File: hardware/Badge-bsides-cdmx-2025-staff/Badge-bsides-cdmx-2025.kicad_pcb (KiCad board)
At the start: 2 copper layers, 50 x 110 mm, 30 parts, among them J1 SWDIO, J3 ADDON, J4 Conn_01x04_Pin, J5 I2C, J6 Conn_01x04_Pin, P6 USB_C_Plug_USB2.0, Q3 DMG3415U-7, SW11 ON, SW2 RESET, U1 PY32F030F28U6TR, U6 AP2112K-3.3

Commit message: feat(Hw):started_routing
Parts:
- added C67: 10uF, Capacitor_SMD:C_0603_1608Metric, B.Cu at (138.6, 53.6)
- added C68: 10uF, Capacitor_SMD:C_0603_1608Metric, B.Cu at (130.4, 73.0)
- added C69: 10uF, Capacitor_SMD:C_0603_1608Metric, B.Cu at (122.8, 54.7)
- added C70: 10uF, Capacitor_SMD:C_0603_1608Metric, B.Cu at (115.0, 74.5)
- added R5: 10k, Resistor_SMD:R_0603_1608Metric, B.Cu at (138.6, 55.1)
- added R6: 10k, Resistor_SMD:R_0603_1608Metric, B.Cu at (130.4, 74.5)
- added R7: 10k, Resistor_SMD:R_0603_1608Metric, B.Cu at (122.8, 53.2)
- added R8: 10k, Resistor_SMD:R_0603_1608Metric, B.Cu at (115.0, 73.0)
- added SW10: SW_Push, Footprints:TS1088R02026, F.Cu at (115.1, 73.7)
- added SW7: SW_Push, Footprints:TS1088R02026, F.Cu at (122.8, 54.1)
- added SW8: SW_Push, Footprints:TS1088R02026, F.Cu at (138.6, 54.2)
- added SW9: SW_Push, Footprints:TS1088R02026, F.Cu at (130.5, 73.7)
- added kibuzzard-6841BD6C: G***, kibuzzard-6841BD6C, B.Cu at (129.0, 141.0)
- BT3, BT4: moved to B.Cu
- J3: moved to F.Cu
- J4: footprint Connector_PinHeader_2.54mm:PinHeader_1x04_P2.54mm_Vertical -> Connector_PinHeader_2.54mm:PinHeader_1x04_P2.54mm_Horizontal; moved to B.Cu
- J6: footprint Connector_PinHeader_2.54mm:PinHeader_1x04_P2.54mm_Vertical -> Connector_PinSocket_2.54mm:PinSocket_1x04_P2.54mm_Horizontal; moved to B.Cu
- moved J1 64.0 mm to (107.9, 84.3)
- moved J3 39.5 mm to (110.9, 46.0), turned to 90 degrees
- moved R4 23.4 mm to (135.2, 81.9)
- moved SW2 23.4 mm to (130.1, 83.4)
- moved C6 23.4 mm to (127.3, 79.6)
- moved J4 23.1 mm to (150.3, 97.5)
- moved J5 21.6 mm to (107.9, 60.7)
- moved R9 20.5 mm to (122.3, 118.5), turned to 0 degrees
- moved R10 20.1 mm to (110.7, 115.8)
- moved R41 20.1 mm to (149.2, 103.9)
- moved U1 20.1 mm to (129.6, 92.4)
- moved C10 20.1 mm to (117.7, 109.2)
- moved C26 20.1 mm to (122.0, 107.7)
- moved Q3 20.1 mm to (113.6, 115.9)
- moved SW11 20.1 mm to (108.4, 110.2)
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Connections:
- J3 pad 5: /GPIO1 -> /GPIO2
- J3 pad 6: /GPIO2 -> /GPIO1
- J4 pad 1: /RX -> GND
- J4 pad 2: /RX -> GND
- J4 pad 3: GND -> /RX
- J4 pad 4: GND -> /RX
- J6 pad 1: /TX -> GND
- J6 pad 2: /TX -> GND
- J6 pad 3: GND -> /TX
- J6 pad 4: GND -> /TX
- U1 pad 1: unconnected-(U1-PA5-Pad1) -> /BTTN2
- U1 pad 10: unconnected-(U1-PB6-Pad10) -> /LED1
- U1 pad 16: /GPIO2 -> /BTTN4
- U1 pad 17: /GPIO1 -> /BTTN3
- U1 pad 2: /LED1 -> /BTTN1
- U1 pad 20: unconnected-(U1-PA4-Pad20) -> /LED2
- U1 pad 3: /LED2 -> /GPIO1
- U1 pad 5: unconnected-(U1-PA12-Pad5) -> /GPIO2
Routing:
- net /BTTN3: track 0.00 -> 43.4 mm, vias 0 -> 1
- net VBUS: track 7.00 -> 40.2 mm, vias 0 -> 2
- net /BTTN2: track 0.00 -> 32.3 mm, vias 0 -> 2
- net /BTTN4: track 0.00 -> 31.3 mm, vias 0 -> 1
- net /LED2: track 0.00 -> 26.1 mm
- net /NTST: track 0.00 -> 25.0 mm, vias 0 -> 2
- net /BTTN1: track 0.00 -> 23.1 mm, vias 0 -> 1
- net /TX: track 0.00 -> 8.26 mm, vias 0 -> 1
- net /SDA: track 0.00 -> 6.40 mm, vias 0 -> 1
- net Net-(D4-K): track 3.60 -> 9.51 mm
- net Net-(D10-K): track 0.00 -> 3.98 mm
- net GND: track 0.00 -> 1.70 mm
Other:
- board size 50 x 110 mm -> 50.1 x 110 mm

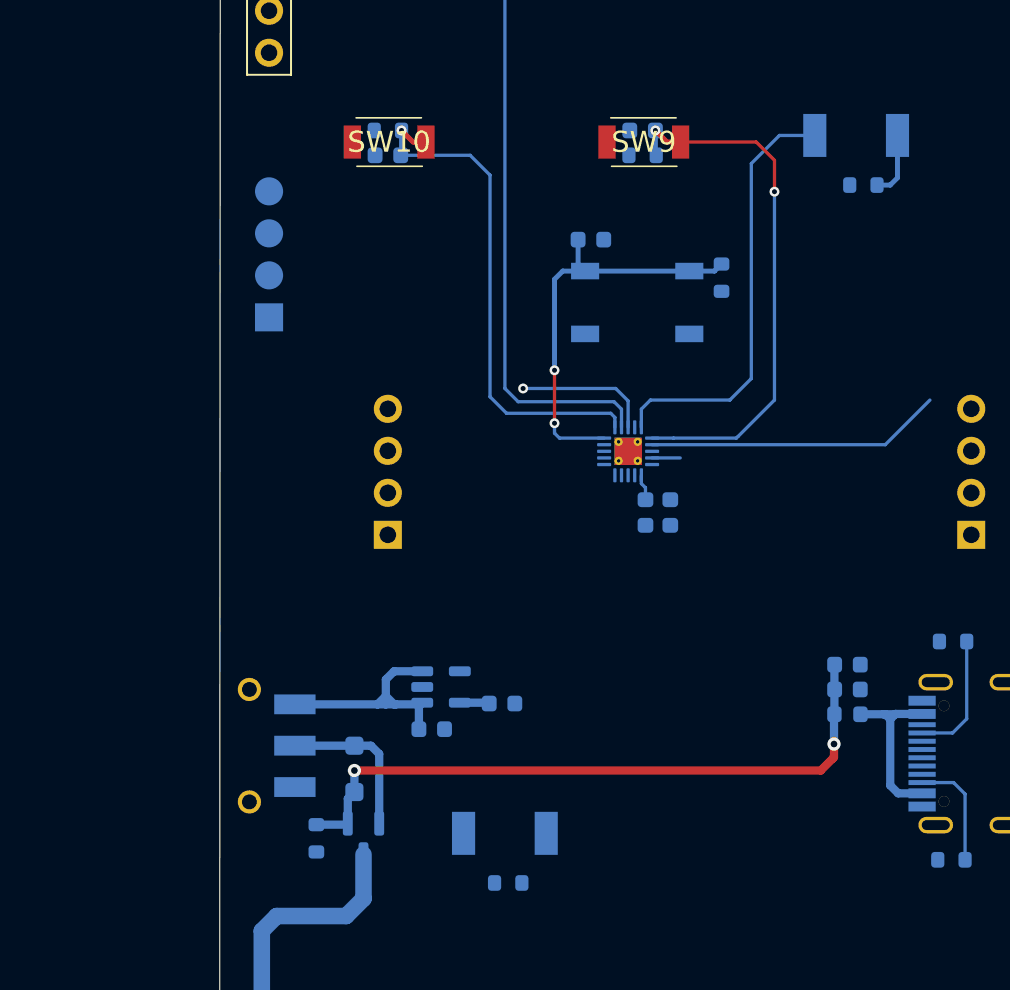
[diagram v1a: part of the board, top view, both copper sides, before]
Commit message: feat(Hw):Neopixels_Added_Staff
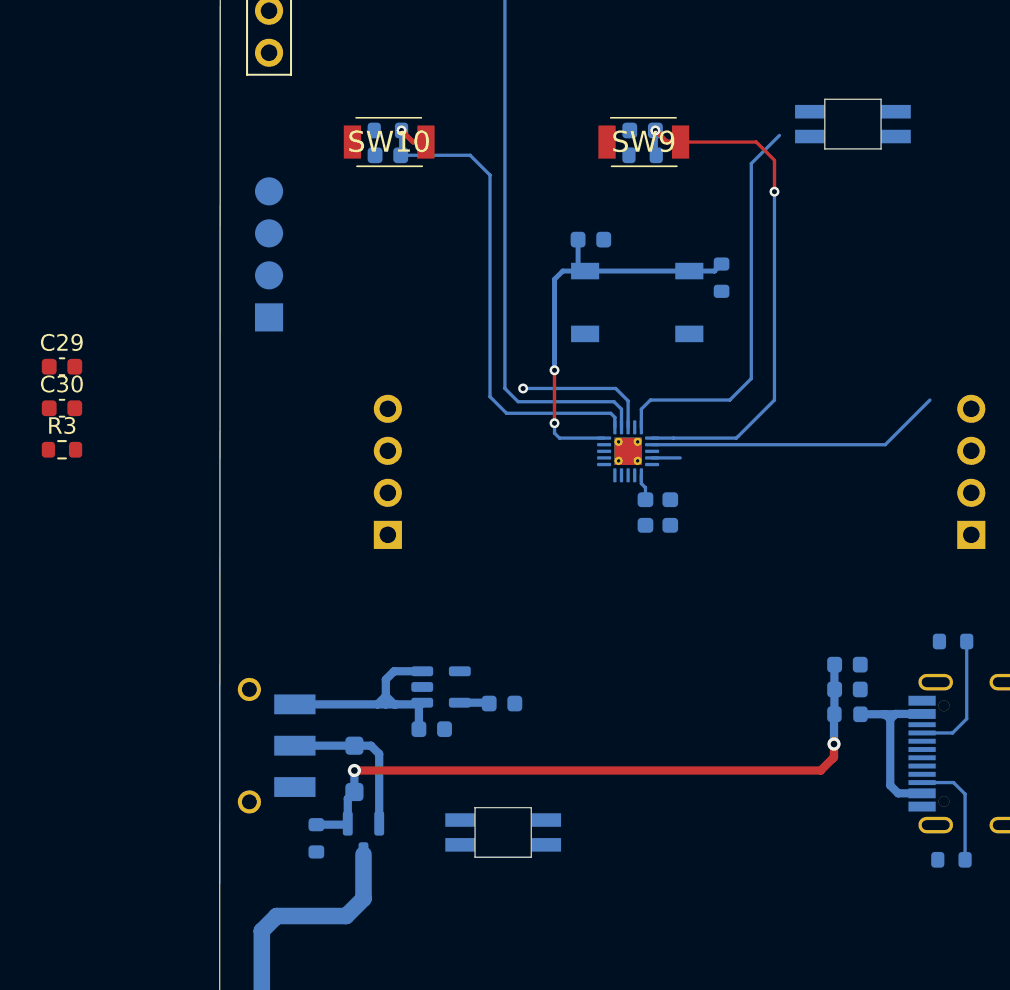
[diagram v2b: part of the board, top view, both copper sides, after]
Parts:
- removed D10, D9: R_LED, Footprints:LYT77K-K2M1
- removed R11, R9: 220, Resistor_SMD:R_0603_1608Metric
- added C29: 100nF, Capacitor_SMD:C_0603_1608Metric, F.Cu at (95.3, 87.3)
- added C30: 100nF, Capacitor_SMD:C_0603_1608Metric, F.Cu at (95.3, 89.8)
- added D19: WS2812B, Footprints:LED_SK6812-E, B.Cu at (143.2, 72.6)
- added D20: WS2812B, Footprints:LED_SK6812-E, B.Cu at (122.0, 115.5)
- added R3: 1K, Resistor_SMD:R_0603_1608Metric, F.Cu at (95.3, 92.3)
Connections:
- BT3 pad 1: Net-(BT3--) -> +BATT
- BT3 pad 2: +BATT -> Net-(BT3--)
- C26 pad 1: +3V3 -> +3.3V
- J3 pad 1: +3V3 -> +3.3V
- R4 pad 2: +3V3 -> +3.3V
- R5 pad 2: +3V3 -> +3.3V
- R6 pad 2: +3V3 -> +3.3V
- R7 pad 2: +3V3 -> +3.3V
- R8 pad 2: +3V3 -> +3.3V
- U1 pad 11: unconnected-(U1-PB7-Pad11) -> /GPIO1
- U1 pad 3: /GPIO1 -> /NEO
- U6 pad 5: +3V3 -> +3.3V
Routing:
- net Net-(D10-K): track 3.98 -> 0.00 mm
- net /LED2: track 26.1 -> 23.9 mm
- net +3V3: track 1.80 -> 0.00 mm
- net +3.3V: track 1.65 -> 3.44 mm

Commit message: feat(HW):Staff_Updated
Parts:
- added kibuzzard-684362A9: G***, kibuzzard-684362A9, B.Cu at (110.5, 105.1)
- added kibuzzard-684362BF: G***, kibuzzard-684362BF, B.Cu at (108.6, 116.2)
- added kibuzzard-684362CB: G***, kibuzzard-684362CB, B.Cu at (114.7, 100.8)
- added kibuzzard-684362D8: G***, kibuzzard-684362D8, B.Cu at (151.2, 100.8)
- added kibuzzard-684362E4: G***, kibuzzard-684362E4, B.Cu at (148.1, 61.6)
- C29, C30, R3: moved to B.Cu
- moved R3 57.0 mm to (148.5, 71.6), turned to 180 degrees
- moved C29 48.7 mm to (140.9, 70.1)
- moved BT4 44.7 mm to (107.4, 142.9), turned to 0 degrees
- moved C30 32.9 mm to (118.8, 113.0), turned to 180 degrees
- moved SW2 31.1 mm to (147.7, 57.8)
- moved SW8 26.9 mm to (145.4, 80.2)
- moved SW7 26.2 mm to (124.6, 80.2), turned to 0 degrees
- moved C6 25.2 mm to (144.9, 61.5)
- moved C67 23.8 mm to (148.2, 75.4)
- moved R5 23.8 mm to (148.2, 76.9)
- moved R7 21.9 mm to (122.4, 75.1), turned to 180 degrees
- moved C69 21.9 mm to (122.5, 76.6), turned to 180 degrees
- moved R4 21.2 mm to (144.9, 63.1), turned to 0 degrees
- moved SW9 7.91 mm to (135.0, 80.2)
- moved C68 6.70 mm to (136.7, 75.4)
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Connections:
- BT4 pad 1: GND -> Net-(BT3--)
- BT4 pad 2: Net-(BT3--) -> GND
- J4 pad 3: /RX -> /TX
- J4 pad 4: /RX -> /TX
- J6 pad 3: /TX -> /RX
- J6 pad 4: /TX -> /RX
- U1 pad 10: /LED1 -> unconnected-(U1-PB6-Pad10)
- U1 pad 12: unconnected-(U1-PF4/BOOT0-Pad12) -> /GPIO2
- U1 pad 20: /LED2 -> unconnected-(U1-PA4-Pad20)
- U1 pad 5: /GPIO2 -> unconnected-(U1-PA12-Pad5)
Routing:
- net +3.3V: track 3.44 -> 171.4 mm, vias 0 -> 6
- net /GPIO2: track 0.00 -> 77.8 mm, vias 0 -> 1
- net /GPIO1: track 0.00 -> 69.9 mm, vias 0 -> 1
- net /SCL: track 0.03 -> 64.2 mm
- net /SDA: track 6.40 -> 69.2 mm, vias 1 -> 0
- net Net-(D19-DOUT): track 0.00 -> 55.8 mm, vias 0 -> 2
- net Net-(BT3--): track 55.1 -> 14.1 mm
- net VBUS: track 40.2 -> 80.8 mm
- net /NEO: track 0.00 -> 39.8 mm
- net /NTST: track 25.0 -> 62.5 mm
- net /SWCLK: track 0.00 -> 37.0 mm
- net /SWDIO: track 0.00 -> 36.7 mm
- net +BATT: track 16.9 -> 51.2 mm
- net /LED2: track 23.9 -> 0.00 mm
- net /RX: track 0.00 -> 19.2 mm, vias 0 -> 1
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- added copper zone on B.Cu, net GND
- added copper zone on F.Cu, net GND
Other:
- board size 50.1 x 110 mm -> 49.9 x 109.8 mm

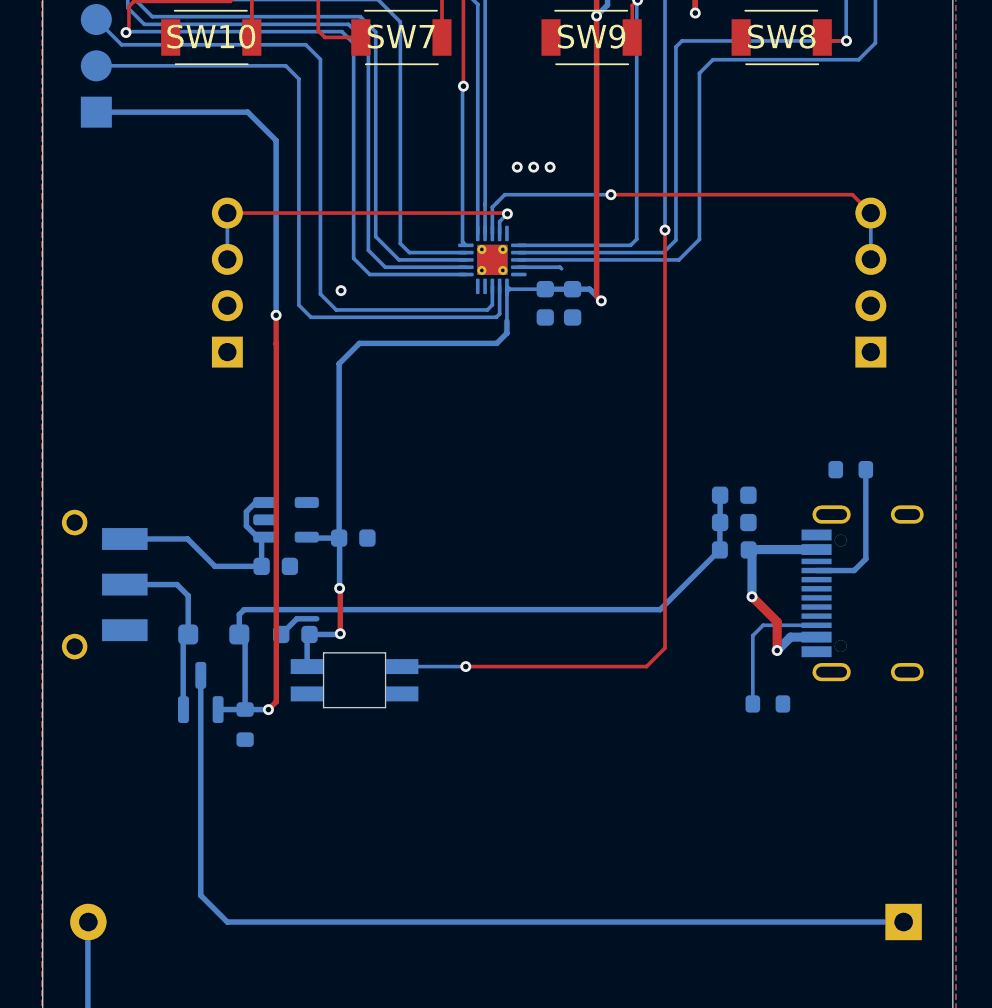
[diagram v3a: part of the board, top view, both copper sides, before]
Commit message: fix(Hw):Connectors_Moved
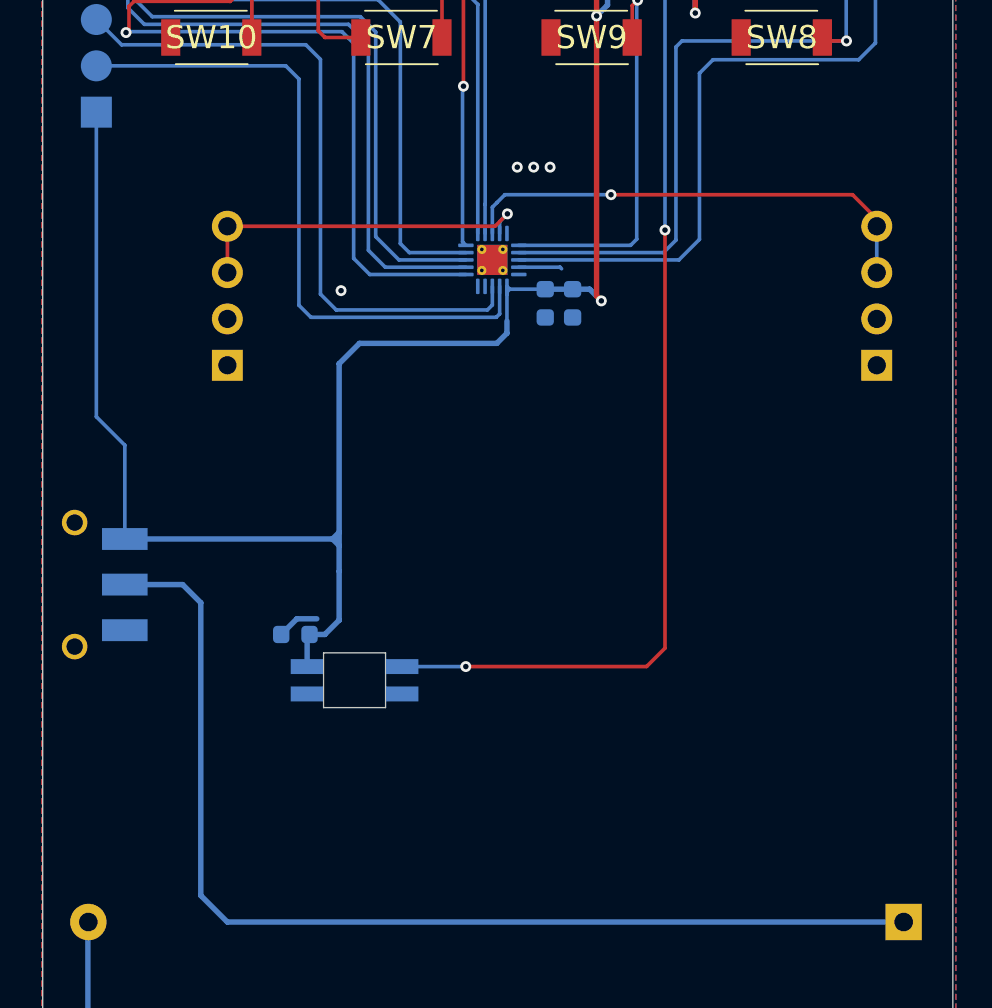
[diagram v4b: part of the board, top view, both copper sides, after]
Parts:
- removed C10, C26, C27: 10uF, Capacitor_SMD:C_0603_1608Metric
- removed C33: 100nF, Capacitor_SMD:C_0603_1608Metric
- removed D4: MBR120, Diode_SMD:D_SOD-123F
- removed F3: 750mA, Fuse:Fuse_0603_1608Metric
- removed P6: USB_C_Plug_USB2.0, Footprints:C393939
- removed Q3: DMG3415U-7, Package_TO_SOT_SMD:SOT-23
- removed R10: 100K, Resistor_SMD:R_0603_1608Metric
- removed R41, R45: 5k1, Resistor_SMD:R_0603_1608Metric
- removed U6: AP2112K-3.3, Package_TO_SOT_SMD:SOT-23-5
- moved J4 0.79 mm to (150.7, 98.2)
- moved J6 0.72 mm to (115.0, 98.2)
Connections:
- J1 pad 1: VBUS -> +3.3V
- SW11 pad 2: Net-(D4-K) -> +BATT
- SW11 pad 3: Net-(SW11-A) -> +3.3V
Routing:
- net VBUS: track 80.8 -> 0.00 mm, vias 2 -> 0
- net +3.3V: track 171.4 -> 205.6 mm, vias 6 -> 4
- net Net-(SW11-A): track 13.1 -> 0.00 mm
- net Net-(F3-Pad1): track 12.4 -> 0.00 mm, vias 2 -> 0
- net Net-(D4-K): track 10.1 -> 0.00 mm
- net +BATT: track 51.2 -> 59.8 mm
- net Net-(P6-CC): track 7.86 -> 0.00 mm
- net Net-(P6-VCONN): track 7.48 -> 0.00 mm

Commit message: fix(Hw):Labels_Updated
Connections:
- U1 pad 21: (no net) -> GND
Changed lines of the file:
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@@
 			)
 		)
-		(property "#LCSC" "C455280"
+		(property "#LCSC" ""
 			(at 0 0 0)
 			(unlocked yes)
@@
 			)
 		)
+		(property "LCSC#" "C455280"
+			(at 0 0 0)
+			(unlocked yes)
+			(layer "F.Fab")
+			(hide yes)
+			(effects
+				(font
+					(size 1 1)
+					(thickness 0.15)
+				)
+			)
+		)
 		(sheetname "/")
 		(sheetfile "Badge-bsides-cdmx-2025.kicad_sch")
@@
 			)
 		)
-		(property "#LCSC" "C455280"
+		(property "#LCSC" ""
 			(at 0 0 0)
 			(unlocked yes)
@@
 			)
 		)
+		(property "LCSC#" "C455280"
+			(at 0 0 0)
+			(unlocked yes)
+			(layer "F.Fab")
+			(hide yes)
+			(effects
+				(font
+					(size 1 1)
+					(thickness 0.15)
+				)
+			)
+		)
 		(sheetname "/")
 		(sheetfile "Badge-bsides-cdmx-2025.kicad_sch")
@@
 			)
 		)
-		(property "#LCSC" "C455280"
+		(property "#LCSC" ""
 			(at 0 0 0)
 			(unlocked yes)
@@
 			)
 		)
+		(property "LCSC#" "C455280"
+			(at 0 0 0)
+			(unlocked yes)
+			(layer "F.Fab")
+			(hide yes)
+			(effects
+				(font
+					(size 1 1)
+					(thickness 0.15)
+				)
+			)
+		)
 		(sheetname "/")
 		(sheetfile "Badge-bsides-cdmx-2025.kicad_sch")
@@
 			)
 		)
-		(property "#LCSC" "C455280"
+		(property "#LCSC" ""
 			(at 0 0 0)
 			(unlocked yes)
@@
 			)
 		)
+		(property "LCSC#" "C455280"
+			(at 0 0 0)
+			(unlocked yes)
+			(layer "F.Fab")
+			(hide yes)
+			(effects
+				(font
+					(size 1 1)
+					(thickness 0.15)
+				)
+			)
+		)
 		(sheetname "/")
 		(sheetfile "Badge-bsides-cdmx-2025.kicad_sch")
@@
 			(layers "*.Cu")
 			(remove_unused_layers no)
+			(net 1 "GND")
+			(pinfunction "VSS")
+			(pintype "bidirectional")
 		)
 		(pad "21" thru_hole circle
@@
 			(layers "*.Cu")
 			(remove_unused_layers no)
+			(net 1 "GND")
+			(pinfunction "VSS")
+			(pintype "bidirectional")
 		)
 		(pad "21" smd rect
@@
 			(property pad_prop_heatsink)
 			(layers "F.Cu")
+			(net 1 "GND")
+			(pinfunction "VSS")
+			(pintype "bidirectional")
 			(zone_connect 2)
 		)
@@
 			(property pad_prop_heatsink)
 			(layers "B.Cu" "B.Mask")
+			(net 1 "GND")
+			(pinfunction "VSS")
+			(pintype "bidirectional")
 			(zone_connect 2)
 		)
@@
 			(layers "*.Cu")
 			(remove_unused_layers no)
+			(net 1 "GND")
+			(pinfunction "VSS")
+			(pintype "bidirectional")
 		)
 		(pad "21" thru_hole circle
@@
 			(layers "*.Cu")
 			(remove_unused_layers no)
+			(net 1 "GND")
+			(pinfunction "VSS")
+			(pintype "bidirectional")
 		)
 		(embedded_fonts no)
@@
 			)
 		)
+		(property "LCSC#" "C492412"
+			(at 0 0 0)
+			(unlocked yes)
+			(layer "B.Fab")
+			(hide yes)
+			(effects
+				(font
+					(size 1 1)
+					(thickness 0.15)
+				)
+				(justify mirror)
+			)
+		)
 		(property ki_fp_filters "Connector*:*_1x??_*")
 		(sheetname "/")
@@
 			)
 		)
-		(property "LCSC#" "C478888"
+		(property "LCSC#" "C66501"
 			(at 0 0 0)
 			(unlocked yes)
@@
 			)
 		)
-		(property "#LCSC" "C96446"
+		(property "#LCSC" ""
 			(at 0 0 0)
 			(unlocked yes)
@@
 			)
 		)
+		(property "LCSC#" "C96446"
+			(at 0 0 180)
+			(unlocked yes)
+			(layer "B.Fab")
+			(hide yes)
+			(effects
+				(font
+					(size 1 1)
+					(thickness 0.15)
+				)
+				(justify mirror)
+			)
+		)
 		(property ki_fp_filters "C_*")
 		(sheetname "/")
@@
 			)
 		)
-		(property "#LCSC" "C96446"
+		(property "#LCSC" ""
 			(at 0 0 0)
 			(unlocked yes)
@@
 			)
 		)
+		(property "LCSC#" "C96446"
+			(at 0 0 180)
+			(unlocked yes)
+			(layer "B.Fab")
+			(hide yes)
+			(effects
+				(font
+					(size 1 1)
+					(thickness 0.15)
+				)
+				(justify mirror)
+			)
+		)
 		(property ki_fp_filters "C_*")
 		(sheetname "/")
@@
 			)
 		)
-		(property "LCSC#" "C85713"
+		(property "LCSC#" "C96446"
 			(at 0 0 90)
 			(unlocked yes)
@@
 			)
 		)
-		(property "LCSC#" "C22548"
+		(property "LCSC#" "C114669 "
 			(at 0 0 0)
 			(unlocked yes)
@@
 			)
 		)
-		(property "LCSC#" "C478888"
+		(property "LCSC#" "C66501"
 			(at 0 0 180)
 			(unlocked yes)
@@
 			)
 		)
+		(property "LCSC#" "C2897386"
+			(at 0 0 0)
+			(unlocked yes)
+			(layer "B.Fab")
+			(hide yes)
+			(effects
+				(font
+					(size 1 1)
+					(thickness 0.15)
+				)
+				(justify mirror)
+			)
+		)
 		(property ki_fp_filters "Connector*:*_1x??_*")
 		(sheetname "/")
@@
 			)
 		)
-		(property "LCSC#" "C14663"
+		(property "LCSC#" "C66501"
 			(at 0 0 90)
 			(unlocked yes)
@@
 			)
 		)
-		(property "#LCSC" "C96446"
+		(property "#LCSC" ""
 			(at 0 0 0)
 			(unlocked yes)
@@
 			)
 		)
+		(property "LCSC#" "C96446"
+			(at 0 0 180)
+			(unlocked yes)
+			(layer "B.Fab")
+			(hide yes)
+			(effects
+				(font
+					(size 1 1)
+					(thickness 0.15)
+				)
+				(justify mirror)
+			)
+		)
 		(property ki_fp_filters "C_*")
 		(sheetname "/")
@@
 			)
 		)
-		(property "#LCSC" "C96446"
+		(property "#LCSC" ""
 			(at 0 0 0)
 			(unlocked yes)
@@
 			)
 		)
+		(property "LCSC#" "C96446"
+			(at 0 0 180)
+			(unlocked yes)
+			(layer "B.Fab")
+			(hide yes)
+			(effects
+				(font
+					(size 1 1)
+					(thickness 0.15)
+				)
+				(justify mirror)
+			)
+		)
 		(property ki_fp_filters "C_*")
 		(sheetname "/")
@@
 			)
 		)
-		(property "LCSC#" "-"
+		(property "LCSC#" "C221660"
 			(at 0 0 270)
 			(unlocked yes)
@@
 			)
 		)
-		(property "Manufacturer_Part_Number" "JS102011SAQN"
+		(property "Manufacturer_Part_Number" ""
 			(at 0 0 270)
 			(unlocked yes)
